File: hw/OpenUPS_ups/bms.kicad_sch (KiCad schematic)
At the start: 52 parts, among them Q1103 BSS84, Q1104 BSS84, Q1107 BSS84, Q601 2N7002, Q601 AON7534, U1101 BQ76920PW, U901 π220N31

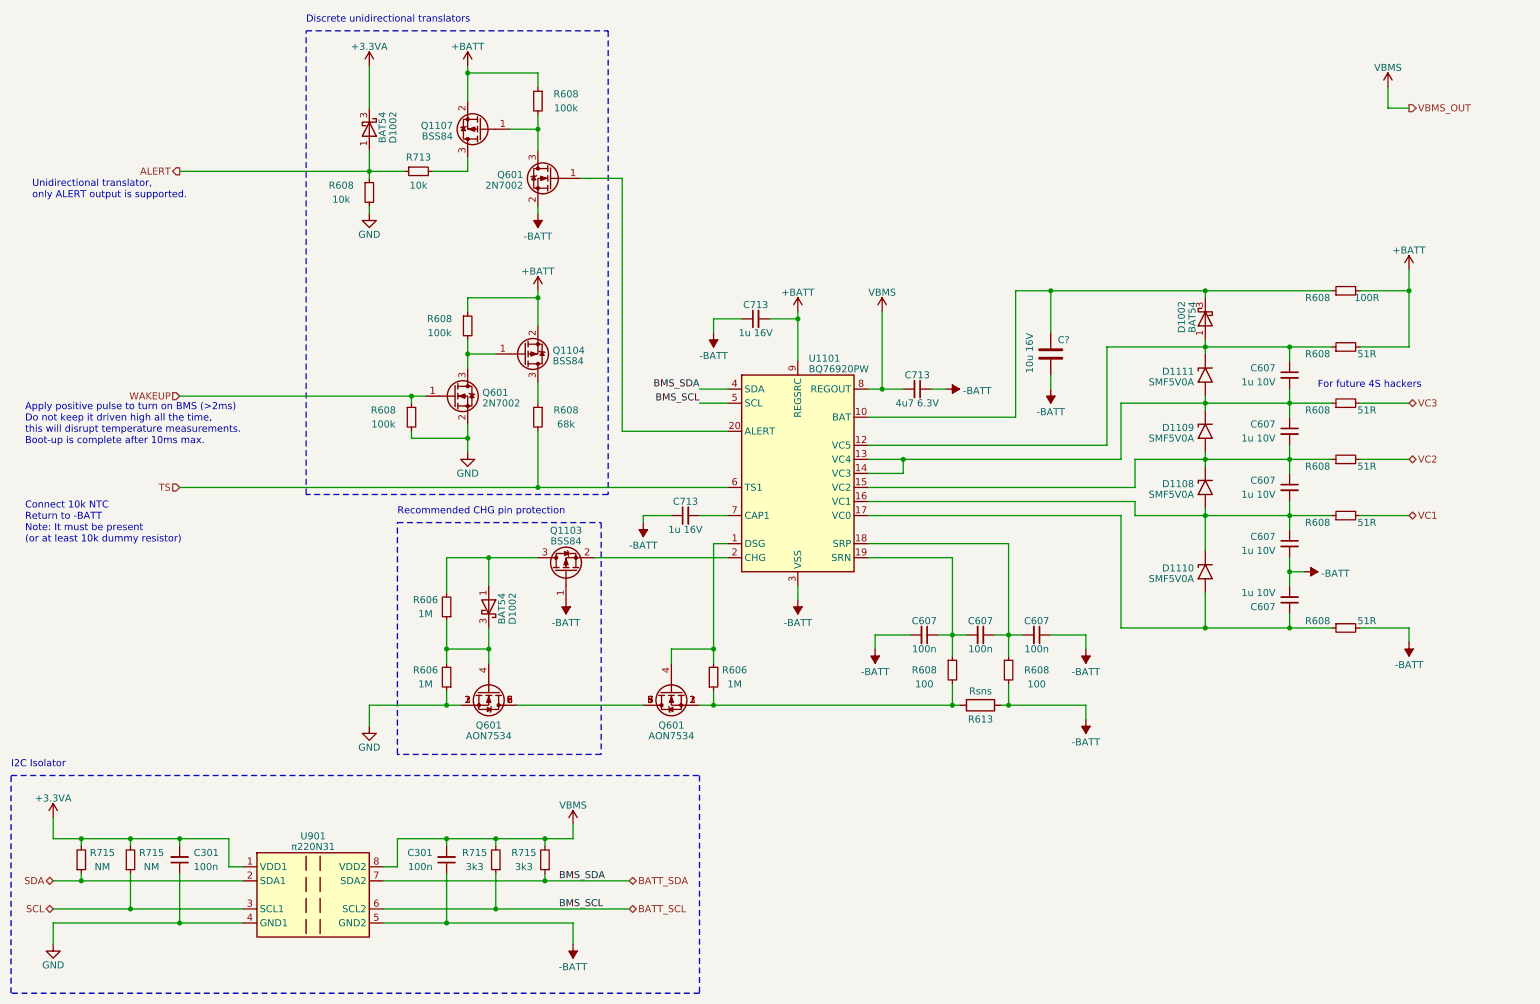
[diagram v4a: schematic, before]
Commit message: BMS placement complete (no routing)
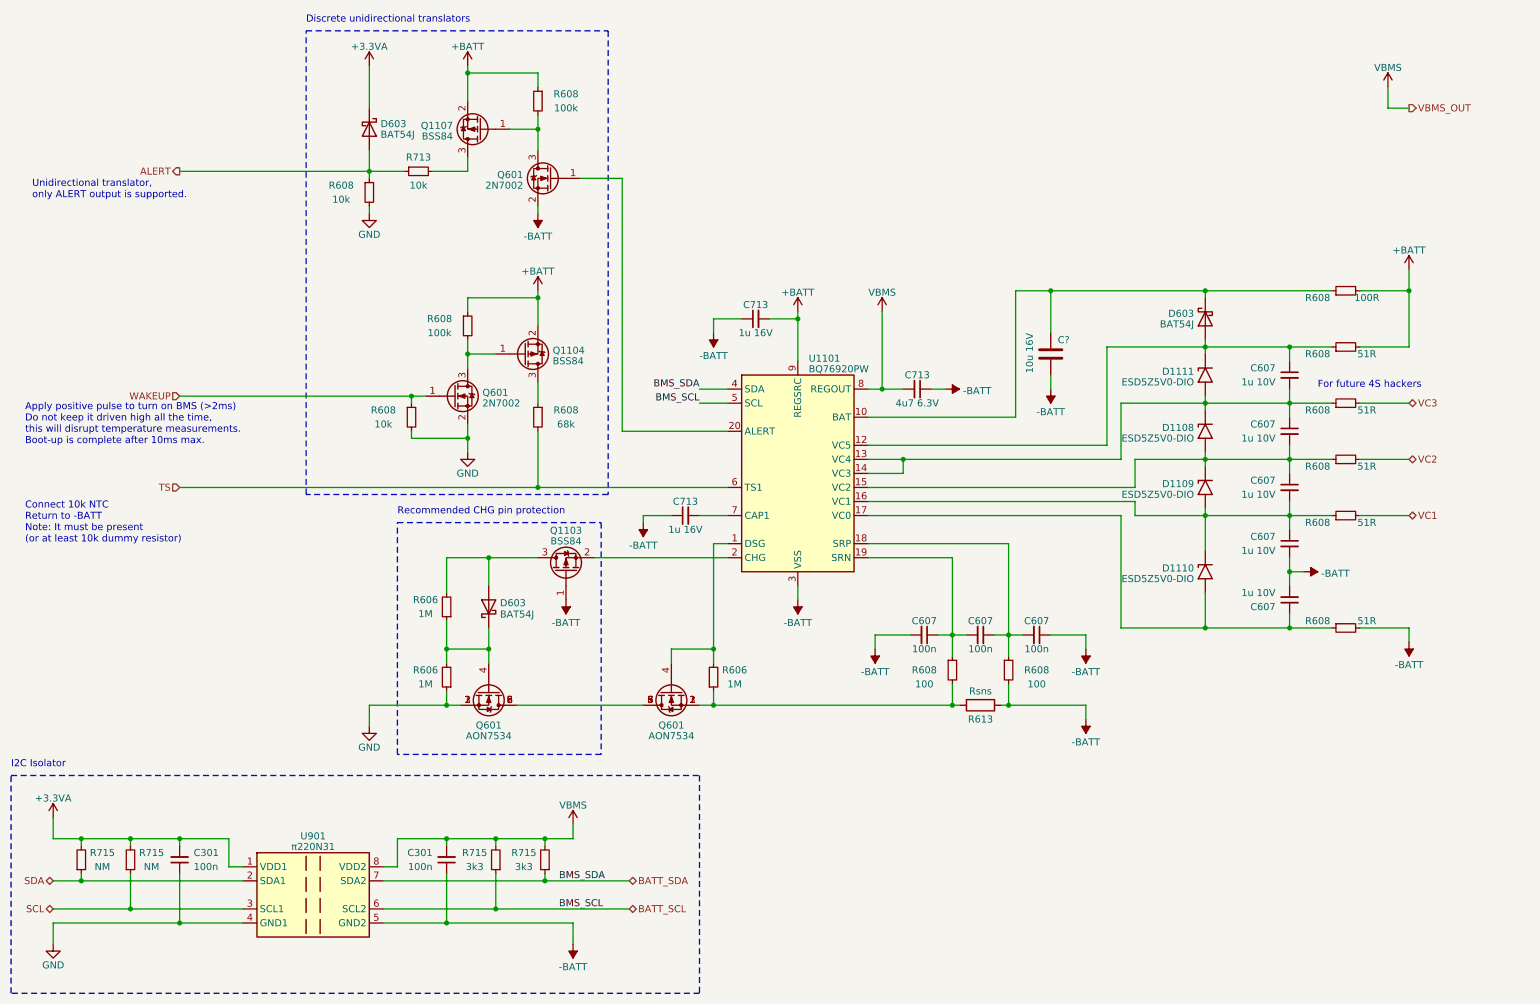
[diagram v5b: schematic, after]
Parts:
- removed D1002 (x3): BAT54, Package_TO_SOT_SMD:SOT-23, symbol Diode:BAT54W
- added D603 (x3): BAT54J, Diode_SMD:D_SOD-323F, symbol Diode:BAT54J
- D1108, D1109, D1110, D1111: value SMF5V0A -> ESD5Z5V0-DIO; footprint Diode_SMD:D_SMF -> Diode_SMD:D_SOD-523
- R608: value 100k -> 10k
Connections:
- net +3.3VA: now also D603.1 (K)
- net ALERT: now also D603.2 (A)
- net at C607.1, D1111.1 (A1), R608.1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: now also D603.2 (A)
- net at C?.1, R608.1, U1101.10 (BAT): now also D603.1 (K)
- net at C607.1, C607.2, D1111.2 (A2)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: now also D1108.1 (A1); no longer D1109.1 (A1)
- net at C607.1, C607.2, R608.1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: now also D1108.2 (A2), D1109.1 (A1); no longer D1108.1 (A1), D1109.2 (A2)
- net at C607.1, C607.2, D1110.1 (A1)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: now also D1109.2 (A2); no longer D1108.2 (A2)
- net at Q601.4 (G), R606.1, R606.2: now also D603.1 (K)
- net at Q1103.3 (D), R606.2: now also D603.2 (A)
